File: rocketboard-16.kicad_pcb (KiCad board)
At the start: 2 copper layers, 86.2 x 105.8 mm, 110 parts, among them J1 SWD, K1 MX_RGB, K10 MX_RGB, K11 MX_RGB, K12 MX_RGB, K13 MX_RGB, K14 MX_RGB, K15 MX_RGB, K16 MX_RGB, K2 MX_RGB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

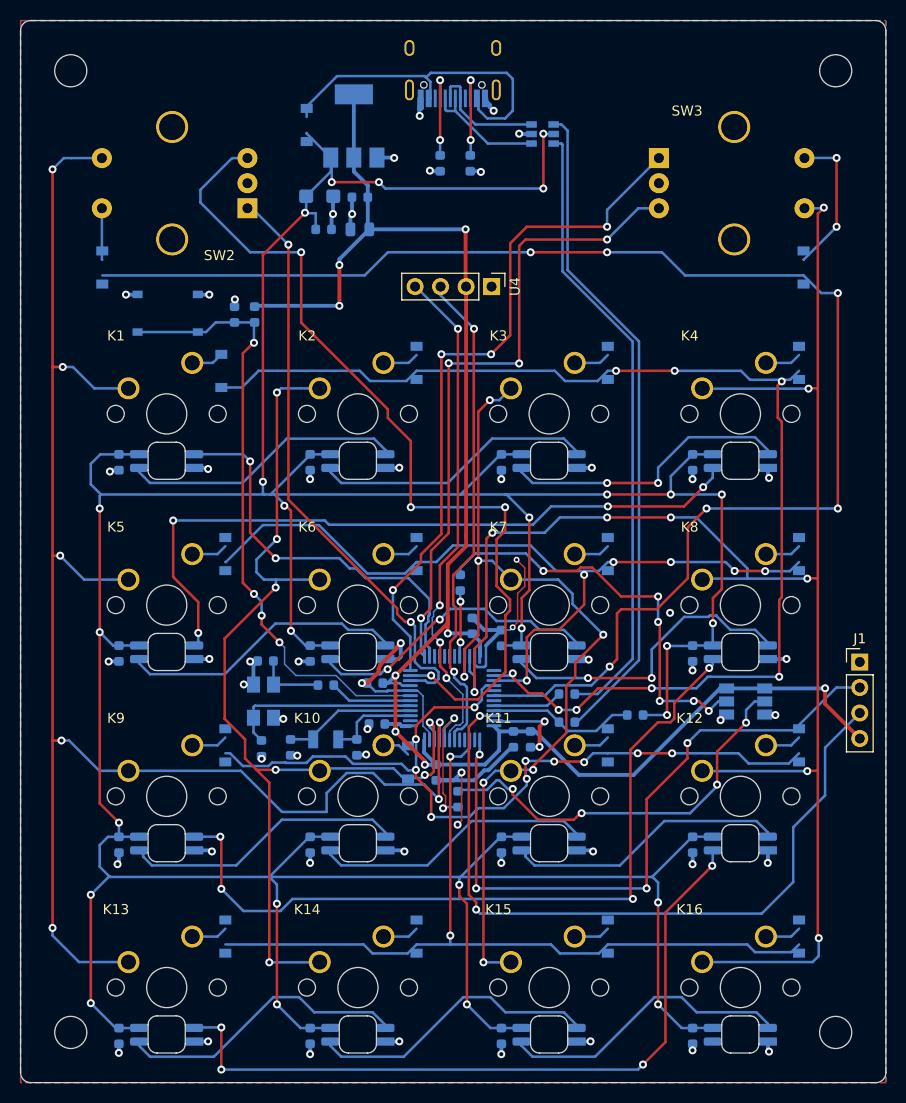
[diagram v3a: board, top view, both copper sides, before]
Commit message: Connected up all the components that changed due to BOM items. Still has one missing fill connection for some reason.
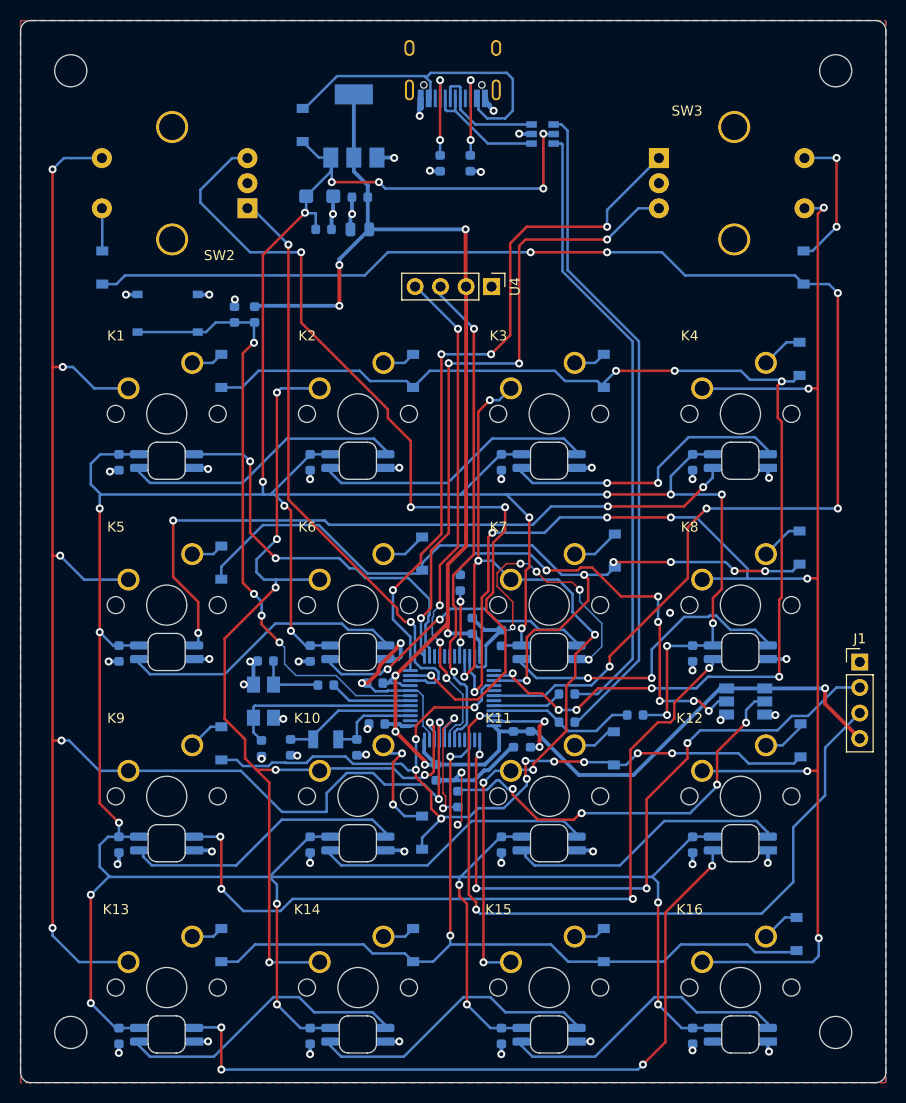
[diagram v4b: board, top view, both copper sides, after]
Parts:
- moved D10 7.14 mm to (120.0, 126.4)
- moved D13 0.94 mm to (100.0, 137.6)
- moved D15 0.94 mm to (138.1, 137.6)
- moved D5 0.94 mm to (100.0, 99.5)
- moved D14 0.92 mm to (119.1, 137.6)
- moved D3 0.89 mm to (138.1, 80.4)
- moved D2 0.87 mm to (119.1, 80.4)
- moved D7 0.78 mm to (139.2, 98.3)
- moved D11 0.67 mm to (139.1, 118.0)
- moved D8 0.65 mm to (157.6, 98.0)
- moved D6 0.55 mm to (120.0, 98.6)
- moved D12 0.52 mm to (157.7, 117.2)
- moved D9 0.45 mm to (100.0, 117.5)
- moved D4 0.40 mm to (157.6, 79.2)
- moved D17 0.40 mm to (108.1, 55.9)
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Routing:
- net GND: track 131.5 -> 148.0 mm, vias 59 -> 61
- net Net-(D10-Pad2): track 2.83 -> 11.0 mm, vias 0 -> 2
- net ROW3: track 82.1 -> 85.9 mm
- net ROW2: track 82.0 -> 85.0 mm
- net Row4: track 81.1 -> 83.0 mm
- net ROW0: track 145.1 -> 143.3 mm
- net ROW1: track 122.3 -> 123.6 mm
- net Net-(D7-Pad2): track 3.63 -> 4.83 mm
- net Net-(D6-Pad2): track 3.63 -> 4.55 mm
- net Net-(D12-Pad2): track 3.63 -> 4.55 mm
- net Net-(D18-Pad2): track 5.13 -> 4.27 mm
- net Net-(D11-Pad2): track 3.63 -> 4.46 mm
- net COL2: track 91.8 -> 91.1 mm
- net Net-(D8-Pad2): track 3.63 -> 4.30 mm
- net Net-(D17-Pad2): track 34.6 -> 34.0 mm
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
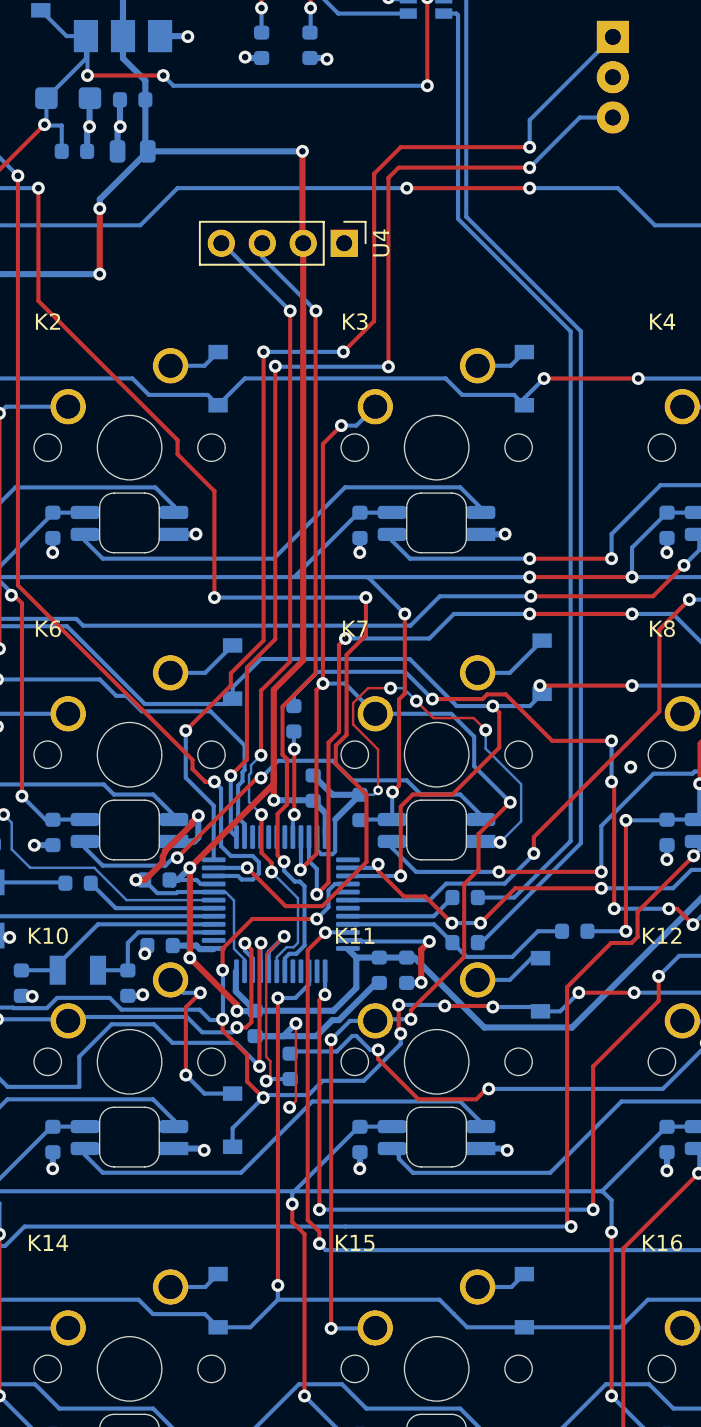
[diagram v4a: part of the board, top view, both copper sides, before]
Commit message: Updated the graphics, added some more, and made some slight changed to some components
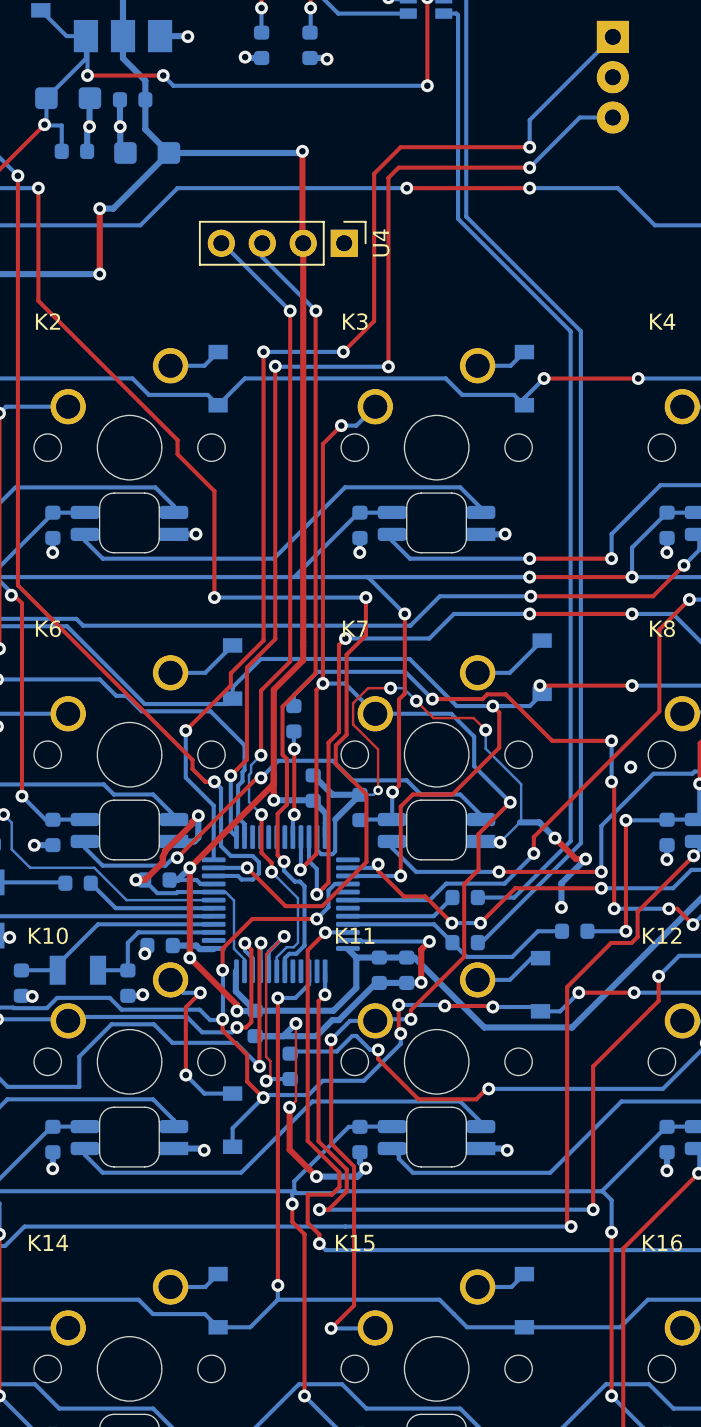
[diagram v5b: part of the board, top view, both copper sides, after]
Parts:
- removed G***: LOGO, seth-logo:saturn_v_simplified
- removed REF**: Board Title, josh-logos:board-title
- added H5: Graphic, seth-logo:saturn_v_simplified, B.Cu at (85.3, 124.8)
- added H6: Board Info, seth-logo:board-title, B.Cu at (84.7, 98.4)
- added H7: Graphic, seth-logo:lunar_module, B.Cu at (143.8, 72.2)
- added H8: Board Info, seth-logo:text, B.Cu at (83.2, 70.4)
- added H9: Graphic, seth-logo:space_shuttle, B.Cu at (161.4, 125.8)
- C13: footprint Capacitor_SMD:C_0805_2012Metric -> Capacitor_Tantalum_SMD:CP_EIA-3216-10_Kemet-I
- moved C13 0.91 mm to (114.7, 66.4)
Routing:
- net GND: track 148.0 -> 167.2 mm, vias 61 -> 65
- net SWDIO: track 74.1 -> 76.6 mm
- net SWCLK: track 67.5 -> 69.3 mm
- net COL2: track 91.1 -> 92.3 mm

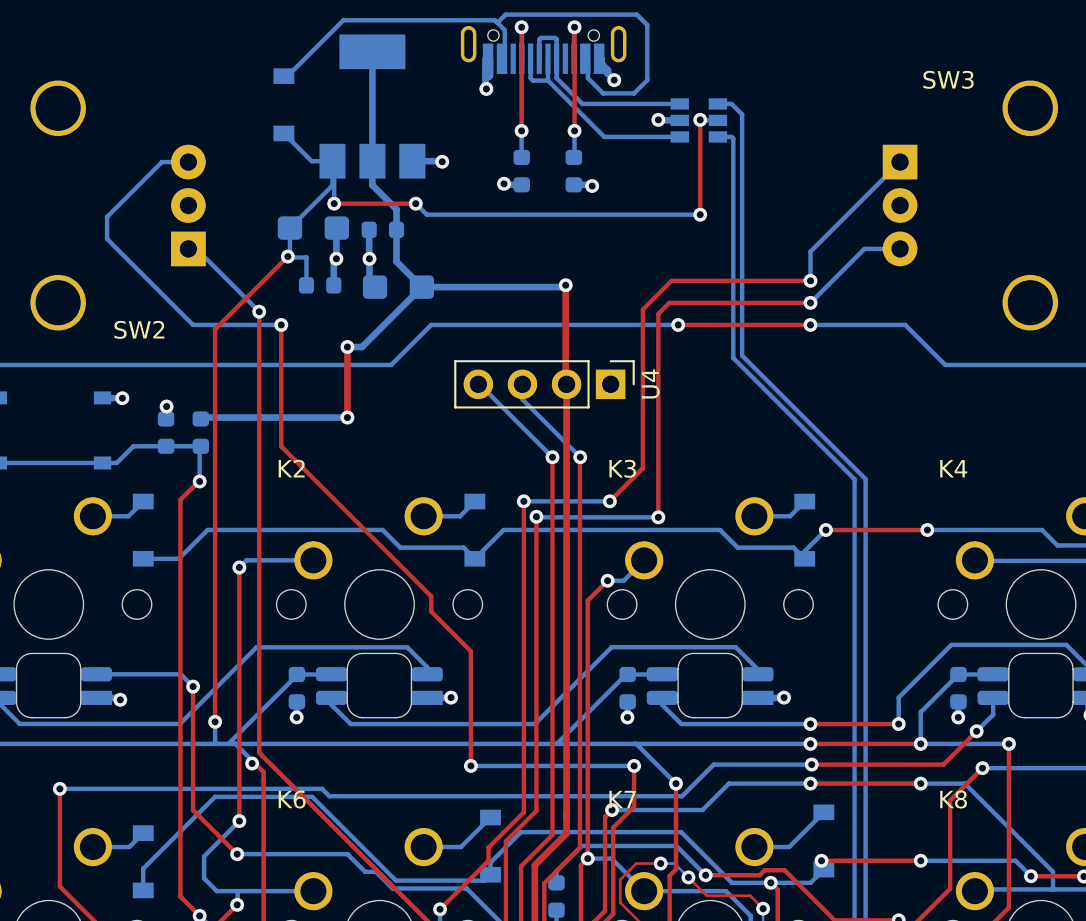
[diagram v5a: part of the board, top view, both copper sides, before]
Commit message: Needed to add debounce and pullups to the rotary encoder lines, added to sch and updated PCB
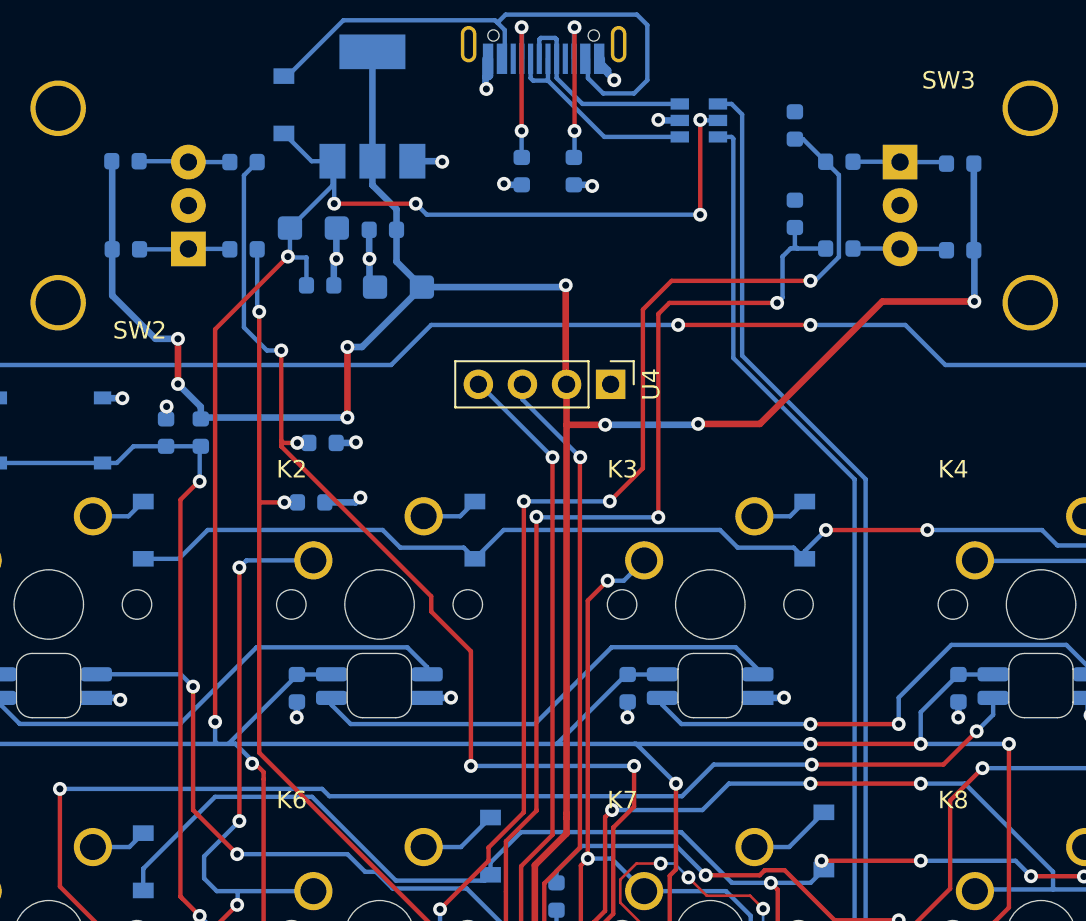
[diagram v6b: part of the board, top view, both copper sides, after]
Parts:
- added C32: 0.1u, Capacitor_SMD:C_0603_1608Metric, B.Cu at (137.5, 62.2)
- added C33: 0.1u, Capacitor_SMD:C_0603_1608Metric, B.Cu at (110.3, 75.4)
- added C34: 0.1u, Capacitor_SMD:C_0603_1608Metric, B.Cu at (137.5, 57.1)
- added C35: 0.1u, Capacitor_SMD:C_0603_1608Metric, B.Cu at (109.7, 78.8)
- added R10: 10k, Resistor_SMD:R_0603_1608Metric, B.Cu at (147.1, 59.3)
- added R11: 10k, Resistor_SMD:R_0603_1608Metric, B.Cu at (99.0, 64.2)
- added R12: 10k, Resistor_SMD:R_0603_1608Metric, B.Cu at (147.1, 64.3)
- added R13: 10k, Resistor_SMD:R_0603_1608Metric, B.Cu at (99.0, 59.1)
- added R14: 10k, Resistor_SMD:R_0603_1608Metric, B.Cu at (140.1, 59.2)
- added R15: 10k, Resistor_SMD:R_0603_1608Metric, B.Cu at (140.1, 64.2)
- added R16: 10k, Resistor_SMD:R_0603_1608Metric, B.Cu at (105.8, 64.2)
- added R17: 10k, Resistor_SMD:R_0603_1608Metric, B.Cu at (105.8, 59.2)
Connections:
- U1 pad 10: EC1_A -> EC1_A_DB
- U1 pad 11: EC1_B -> EC1_B_DB
- U1 pad 12: EC2_A -> EC2_A_DB
- U1 pad 13: EC2_B -> EC2_B_DB
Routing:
- net EC1_B: track 88.2 -> 5.25 mm, vias 4 -> 0
- net EC1_B_DB: track 0.00 -> 81.6 mm, vias 0 -> 5
- net EC2_A_DB: track 0.00 -> 71.7 mm, vias 0 -> 4
- net EC2_A: track 70.3 -> 5.43 mm, vias 4 -> 0
- net EC2_B_DB: track 0.00 -> 63.1 mm, vias 0 -> 4
- net EC1_A_DB: track 0.00 -> 59.5 mm, vias 0 -> 3
- net EC2_B: track 64.7 -> 5.43 mm, vias 4 -> 0
- net EC1_A: track 59.2 -> 5.68 mm, vias 2 -> 0
- net VCC: track 171.3 -> 223.4 mm, vias 8 -> 13
- net GND: track 167.2 -> 170.5 mm, vias 65 -> 67

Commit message: Added hubble, iss, and spacewalk graphics to sch/pcb
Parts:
- added H10: Graphic, seth-logo:iss, B.Cu at (117.5, 68.9)
- added H11: Graphic, seth-logo:spacewalk, B.Cu at (120.2, 91.6)
- added H12: Graphic, seth-logo:hubble_space_telescope, B.Cu at (126.3, 134.2)
